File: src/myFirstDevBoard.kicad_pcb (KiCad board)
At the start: 2 copper layers, 96.5 x 68.6 mm, 36 parts, among them J1 Conn_01x15_Male, J2 Conn_01x15_Male, Q1 BC550, Q2 BC550, Q3 BC550, SW1 SW_Push, SW2 SW_Push, SW3 SW_Push, SW4 SW_Push, SW5 SW_SLIDER, SW6 SW_SLIDER

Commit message: making v0.2
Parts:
- A1: footprint Module:Arduino_Nano -> lib:Arduino_Nano_oval
- BZ1: footprint Buzzer_Beeper:Buzzer_12x9.5RM7.6 -> lib:Buzzer_12x9.5RM7.6_oval
- D1, D2, D3, D4, D5, D6, D7, D8, D9: footprint lib:LED_D5.0mm-4_RGB -> lib:LED_D5.0mm-4_RGB_wide
- R1, R10, R11, R12, R13, R2, R3, R4, R5, R6, R7, R8, R9: footprint Resistor_THT:R_Axial_DIN0207_L6.3mm_D2.5mm_P10.16mm_Horizontal -> lib:R_Axial_DIN0207_L6.3mm_D2.5mm_P10.16mm_Horizontal_oval
- RV1: footprint Potentiometer_THT:Potentiometer_Alps_RK163_Single_Horizontal -> lib:Potentiometer_Alps_RK163_Single_Horizontal_oval
- SW1, SW2, SW3, SW4: footprint Button_Switch_THT:SW_PUSH-12mm -> lib:SW_PUSH-12mm_with_poles
- SW5, SW6: footprint lib:PinHeader_1x03_P2.54mm_Vertical -> lib:PinHeader_1x03_P2.54mm_Vertical_oval
- moved SW5 57.1 mm to (52.1, 62.2)
- moved SW6 53.6 mm to (45.7, 62.2)
- moved BZ1 52.3 mm to (36.8, 63.5)
- moved R12 34.8 mm to (47.0, 54.0), turned to 180 degrees
- moved J1 18.4 mm to (54.6, 47.3)
- moved J2 18.4 mm to (28.1, 11.7)
- moved A1 18.4 mm to (48.7, 47.3)
- moved Q1 1.27 mm to (74.9, 28.6)
- moved Q2 1.27 mm to (85.1, 28.6)
- moved D1 1.27 mm to (74.3, 58.4)
- moved D2 1.27 mm to (84.5, 58.4)
- moved D3 1.27 mm to (94.6, 58.4)
- moved D4 1.27 mm to (74.3, 48.3)
- moved D5 1.27 mm to (84.5, 48.3)
- moved D6 1.27 mm to (94.6, 48.3)
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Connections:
- RV1 pad 2: Net-(RV1-Pad2) -> /pot
- RV1 pad 3: /pot -> GND
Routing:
- net Net-(D3-Pad4): track 76.1 -> 36.2 mm
- net +5V: track 156.2 -> 119.8 mm, vias 0 -> 1
- net /led1: track 14.7 -> 36.2 mm
- net /buzzer: track 46.0 -> 26.2 mm
- net /sw4: track 32.0 -> 50.7 mm
- net /sw1: track 49.1 -> 30.9 mm
- net /led2: track 14.7 -> 32.9 mm
- net /led3: track 12.7 -> 30.3 mm
- net /blue: track 29.2 -> 12.2 mm, vias 1 -> 0
- net /red: track 35.1 -> 51.6 mm
- net /led4: track 11.7 -> 27.8 mm
- net /led5: track 11.4 -> 25.2 mm
- net /sw3: track 23.3 -> 36.7 mm
- net Net-(D2-Pad4): track 43.3 -> 31.3 mm, vias 0 -> 1
- net /sw2: track 35.1 -> 23.9 mm
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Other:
- board text added: "V0.02"
- board text removed: "V0.01"

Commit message: adding v0.03
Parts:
- Q1, Q2, Q3: footprint Package_TO_SOT_THT:TO-92_Inline -> lib:TO-92_Inline_Wide_oval
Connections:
- A1 pad 24: /sw5 -> /led9
- A1 pad 26: /led9 -> /sw5
- J2 pad 11: /led9 -> /sw5
- J2 pad 9: /sw5 -> /led9
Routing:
- net /led9: track 46.5 -> 57.5 mm, vias 2 -> 1
- net /sw5: track 46.3 -> 54.2 mm, vias 2 -> 1
- net +5V: track 119.8 -> 119.3 mm
- net Net-(Q3-Pad2): track 38.9 -> 39.4 mm
- net Net-(Q2-Pad2): track 23.7 -> 24.3 mm
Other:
- board text added: "V0.03"
- board text removed: "V0.02"

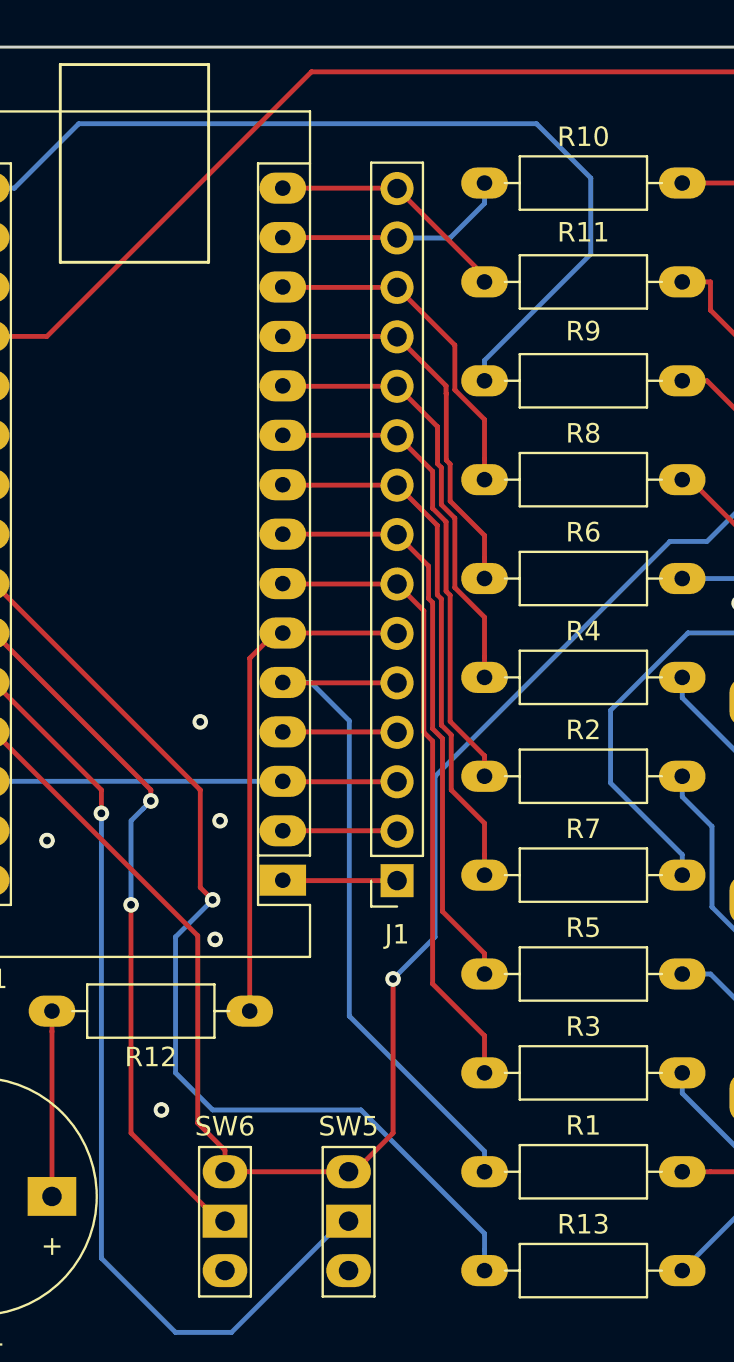
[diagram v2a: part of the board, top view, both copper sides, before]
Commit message: changing silkscreen to be organised
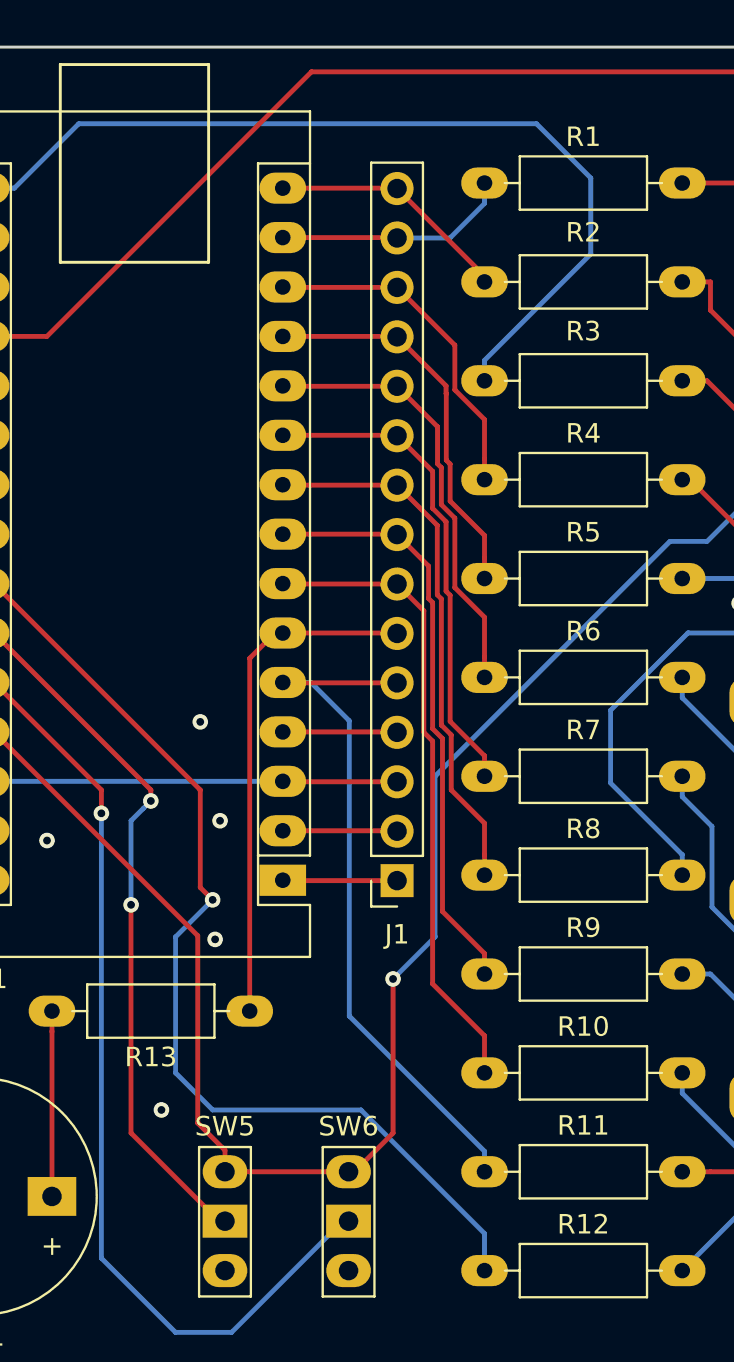
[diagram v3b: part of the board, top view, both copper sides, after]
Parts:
- renumbered R10 to R1, R3 to R10, R1 to R11, R13 to R12, R12 to R13, R11 to R2, R9 to R3, R8 to R4, R6 to R5, R4 to R6, R2 to R7, R7 to R8, R5 to R9, SW6 to SW5, SW5 to SW6
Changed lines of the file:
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@@
     (descr "Resistor, Axial_DIN0207 series, Axial, Horizontal, pin pitch=10.16mm, 0.25W = 1/4W, length*diameter=6.3*2.5mm^2, http://cdn-reichelt.de/documents/datenblatt/B400/1_4W%23YAG.pdf")
     (tags "Resistor Axial_DIN0207 series Axial Horizontal pin pitch 10.16mm 0.25W = 1/4W length 6.3mm diameter 2.5mm")
-    (fp_text reference R1 (at 5.08 -2.37) (layer F.SilkS)
+    (fp_text reference R11 (at 5.08 -2.37) (layer F.SilkS)
       (effects (font (size 1 1) (thickness 0.15)))
     )
@@
     (descr "Resistor, Axial_DIN0207 series, Axial, Horizontal, pin pitch=10.16mm, 0.25W = 1/4W, length*diameter=6.3*2.5mm^2, http://cdn-reichelt.de/documents/datenblatt/B400/1_4W%23YAG.pdf")
     (tags "Resistor Axial_DIN0207 series Axial Horizontal pin pitch 10.16mm 0.25W = 1/4W length 6.3mm diameter 2.5mm")
-    (fp_text reference R2 (at 5.08 -2.37) (layer F.SilkS)
+    (fp_text reference R7 (at 5.08 -2.37) (layer F.SilkS)
       (effects (font (size 1 1) (thickness 0.15)))
     )
@@
     (descr "Resistor, Axial_DIN0207 series, Axial, Horizontal, pin pitch=10.16mm, 0.25W = 1/4W, length*diameter=6.3*2.5mm^2, http://cdn-reichelt.de/documents/datenblatt/B400/1_4W%23YAG.pdf")
     (tags "Resistor Axial_DIN0207 series Axial Horizontal pin pitch 10.16mm 0.25W = 1/4W length 6.3mm diameter 2.5mm")
-    (fp_text reference R3 (at 5.08 -2.37) (layer F.SilkS)
+    (fp_text reference R10 (at 5.08 -2.37) (layer F.SilkS)
       (effects (font (size 1 1) (thickness 0.15)))
     )
@@
     (descr "Resistor, Axial_DIN0207 series, Axial, Horizontal, pin pitch=10.16mm, 0.25W = 1/4W, length*diameter=6.3*2.5mm^2, http://cdn-reichelt.de/documents/datenblatt/B400/1_4W%23YAG.pdf")
     (tags "Resistor Axial_DIN0207 series Axial Horizontal pin pitch 10.16mm 0.25W = 1/4W length 6.3mm diameter 2.5mm")
-    (fp_text reference R4 (at 5.08 -2.37) (layer F.SilkS)
+    (fp_text reference R6 (at 5.08 -2.37) (layer F.SilkS)
       (effects (font (size 1 1) (thickness 0.15)))
     )
@@
     (descr "Resistor, Axial_DIN0207 series, Axial, Horizontal, pin pitch=10.16mm, 0.25W = 1/4W, length*diameter=6.3*2.5mm^2, http://cdn-reichelt.de/documents/datenblatt/B400/1_4W%23YAG.pdf")
     (tags "Resistor Axial_DIN0207 series Axial Horizontal pin pitch 10.16mm 0.25W = 1/4W length 6.3mm diameter 2.5mm")
-    (fp_text reference R5 (at 5.08 -2.37) (layer F.SilkS)
+    (fp_text reference R9 (at 5.08 -2.37) (layer F.SilkS)
       (effects (font (size 1 1) (thickness 0.15)))
     )
@@
     (descr "Resistor, Axial_DIN0207 series, Axial, Horizontal, pin pitch=10.16mm, 0.25W = 1/4W, length*diameter=6.3*2.5mm^2, http://cdn-reichelt.de/documents/datenblatt/B400/1_4W%23YAG.pdf")
     (tags "Resistor Axial_DIN0207 series Axial Horizontal pin pitch 10.16mm 0.25W = 1/4W length 6.3mm diameter 2.5mm")
-    (fp_text reference R6 (at 5.08 -2.37) (layer F.SilkS)
+    (fp_text reference R5 (at 5.08 -2.37) (layer F.SilkS)
       (effects (font (size 1 1) (thickness 0.15)))
     )
@@
     (descr "Resistor, Axial_DIN0207 series, Axial, Horizontal, pin pitch=10.16mm, 0.25W = 1/4W, length*diameter=6.3*2.5mm^2, http://cdn-reichelt.de/documents/datenblatt/B400/1_4W%23YAG.pdf")
     (tags "Resistor Axial_DIN0207 series Axial Horizontal pin pitch 10.16mm 0.25W = 1/4W length 6.3mm diameter 2.5mm")
-    (fp_text reference R7 (at 5.08 -2.37) (layer F.SilkS)
+    (fp_text reference R8 (at 5.08 -2.37) (layer F.SilkS)
       (effects (font (size 1 1) (thickness 0.15)))
     )
@@
     (descr "Resistor, Axial_DIN0207 series, Axial, Horizontal, pin pitch=10.16mm, 0.25W = 1/4W, length*diameter=6.3*2.5mm^2, http://cdn-reichelt.de/documents/datenblatt/B400/1_4W%23YAG.pdf")
     (tags "Resistor Axial_DIN0207 series Axial Horizontal pin pitch 10.16mm 0.25W = 1/4W length 6.3mm diameter 2.5mm")
-    (fp_text reference R8 (at 5.08 -2.37) (layer F.SilkS)
+    (fp_text reference R4 (at 5.08 -2.37) (layer F.SilkS)
       (effects (font (size 1 1) (thickness 0.15)))
     )
@@
     (descr "Resistor, Axial_DIN0207 series, Axial, Horizontal, pin pitch=10.16mm, 0.25W = 1/4W, length*diameter=6.3*2.5mm^2, http://cdn-reichelt.de/documents/datenblatt/B400/1_4W%23YAG.pdf")
     (tags "Resistor Axial_DIN0207 series Axial Horizontal pin pitch 10.16mm 0.25W = 1/4W length 6.3mm diameter 2.5mm")
-    (fp_text reference R9 (at 5.08 2.54 180) (layer F.SilkS)
+    (fp_text reference R3 (at 5.08 2.54 180) (layer F.SilkS)
       (effects (font (size 1 1) (thickness 0.15)))
     )
@@
     (descr "Resistor, Axial_DIN0207 series, Axial, Horizontal, pin pitch=10.16mm, 0.25W = 1/4W, length*diameter=6.3*2.5mm^2, http://cdn-reichelt.de/documents/datenblatt/B400/1_4W%23YAG.pdf")
     (tags "Resistor Axial_DIN0207 series Axial Horizontal pin pitch 10.16mm 0.25W = 1/4W length 6.3mm diameter 2.5mm")
-    (fp_text reference R10 (at 5.08 -2.37) (layer F.SilkS)
+    (fp_text reference R1 (at 5.08 -2.37) (layer F.SilkS)
       (effects (font (size 1 1) (thickness 0.15)))
     )
@@
     (descr "Resistor, Axial_DIN0207 series, Axial, Horizontal, pin pitch=10.16mm, 0.25W = 1/4W, length*diameter=6.3*2.5mm^2, http://cdn-reichelt.de/documents/datenblatt/B400/1_4W%23YAG.pdf")
     (tags "Resistor Axial_DIN0207 series Axial Horizontal pin pitch 10.16mm 0.25W = 1/4W length 6.3mm diameter 2.5mm")
-    (fp_text reference R11 (at 5.08 2.54 180) (layer F.SilkS)
+    (fp_text reference R2 (at 5.08 2.54 180) (layer F.SilkS)
       (effects (font (size 1 1) (thickness 0.15)))
     )
@@
     (descr "Resistor, Axial_DIN0207 series, Axial, Horizontal, pin pitch=10.16mm, 0.25W = 1/4W, length*diameter=6.3*2.5mm^2, http://cdn-reichelt.de/documents/datenblatt/B400/1_4W%23YAG.pdf")
     (tags "Resistor Axial_DIN0207 series Axial Horizontal pin pitch 10.16mm 0.25W = 1/4W length 6.3mm diameter 2.5mm")
-    (fp_text reference R12 (at 5.08 -2.37 180) (layer F.SilkS)
+    (fp_text reference R13 (at 5.08 -2.37 180) (layer F.SilkS)
       (effects (font (size 1 1) (thickness 0.15)))
     )
@@
     (descr "Resistor, Axial_DIN0207 series, Axial, Horizontal, pin pitch=10.16mm, 0.25W = 1/4W, length*diameter=6.3*2.5mm^2, http://cdn-reichelt.de/documents/datenblatt/B400/1_4W%23YAG.pdf")
     (tags "Resistor Axial_DIN0207 series Axial Horizontal pin pitch 10.16mm 0.25W = 1/4W length 6.3mm diameter 2.5mm")
-    (fp_text reference R13 (at 5.08 -2.37) (layer F.SilkS)
+    (fp_text reference R12 (at 5.08 -2.37) (layer F.SilkS)
       (effects (font (size 1 1) (thickness 0.15)))
     )
@@
     (descr "Through hole straight pin header, 1x03, 2.54mm pitch, single row")
     (tags "Through hole pin header THT 1x03 2.54mm single row")
-    (fp_text reference SW5 (at 0 -2.33) (layer F.SilkS)
+    (fp_text reference SW6 (at 0 -2.33) (layer F.SilkS)
       (effects (font (size 1 1) (thickness 0.15)))
     )
@@
     (descr "Through hole straight pin header, 1x03, 2.54mm pitch, single row")
     (tags "Through hole pin header THT 1x03 2.54mm single row")
-    (fp_text reference SW6 (at 0 -2.33) (layer F.SilkS)
+    (fp_text reference SW5 (at 0 -2.33) (layer F.SilkS)
       (effects (font (size 1 1) (thickness 0.15)))
     )
@@
   (segment (start 39.37 43.815) (end 39.37 66.675) (width 0.25) (layer B.Cu) (net 15))
   (segment (start 39.37 66.675) (end 43.18 70.485) (width 0.25) (layer B.Cu) (net 15))
-  (segment (start 28.166554 32.011378) (end 28.145553 32.032379) (width 0.25) (layer F.Cu) (net 43))
-  (segment (start 33.448552 32.011378) (end 28.166554 32.011378) (width 0.25) (layer F.Cu) (net 43))
   (segment (start 48.709553 26.952379) (end 48.688552 26.931378) (width 0.25) (layer F.Cu) (net 16))
   (segment (start 54.561553 26.952379) (end 48.709553 26.952379) (width 0.25) (layer F.Cu) (net 16))
@@
   (segment (start 97.79 22.225) (end 97.79 28.575) (width 0.25) (layer F.Cu) (net 42))
   (segment (start 86.995 11.43) (end 97.79 22.225) (width 0.25) (layer F.Cu) (net 42))
+  (segment (start 28.166554 32.011378) (end 28.145553 32.032379) (width 0.25) (layer F.Cu) (net 43))
+  (segment (start 33.448552 32.011378) (end 28.166554 32.011378) (width 0.25) (layer F.Cu) (net 43))
   (via (at 45.085 48.26) (size 0.8) (drill 0.4) (layers F.Cu B.Cu) (net 43))
   (segment (start 44.45 47.625) (end 45.085 48.26) (width 0.25) (layer F.Cu) (net 43))
